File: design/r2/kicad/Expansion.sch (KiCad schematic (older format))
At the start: 25 parts, among them IC1 MC68010P10, IC4 MC68901P, IC6 74174N, IC9 74LS01N, J1 PWR, J3 Conn_02x32_Odd_Even

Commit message: Complete schematic capture for r2
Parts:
- removed IC4: MC68901P, rosco_m68k:DIL48, symbol rosco_m68k-eagle-import:MC68901P
- removed IC6: 74174N, Package_DIP:DIP-16_W7.62mm_Socket_LongPads, symbol rosco_m68k-eagle-import:74174N
- renumbered J1 to J5
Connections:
- net labels removed: A[1..23], D[0..15], IEO
- wire segments 152 -> 78
- no-connect marks 0 -> 1
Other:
- moved on the sheet: C14, C15, C16, C17, C18, C19, C20, C21, C22, C23, C24, C25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

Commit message: Tidy up footprints
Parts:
- removed IC9: 74LS01N, Package_DIP:DIP-14_W7.62mm_Socket_LongPads, symbol rosco_m68k-eagle-import:7401N
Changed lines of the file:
@@
 $Descr A4 11693 8268
 encoding utf-8
-Sheet 3 7
+Sheet 2 7
 Title "ROSCO_M68K GENERAL PURPOSE MC68010 COMPUTER"
 Date "2021-10-08"
@@
 $EndComp
 $Comp
-L rosco_m68k-eagle-import:7401N IC?
-U 5 1 5F6CD650
-P 7500 5250
-AR Path="/5F6CD650" Ref="IC?"  Part="5"
-AR Path="/5E53B952/5F6CD650" Ref="IC?"  Part="5"
-AR Path="/5E53BC83/5F6CD650" Ref="IC9"  Part="5"
-F 0 "IC9" H 7475 5225 59  0000 L BNN
-F 1 "74LS01N" H 7600 5050 59  0001 L BNN
-F 2 "Package_DIP:DIP-14_W7.62mm_Socket_LongPads" H 7500 5250 50  0001 C CNN
-F 3 "" H 7500 5250 50  0001 C CNN
-	5    7500 5250
-	1    0    0    -1
-$EndComp
-$Comp
 L rosco_m68k-eagle-import:C2,5-3 C?
 U 1 1 5F6CD656
@@
 Wire Wire Line
 	3450 5750 3750 5750
-Wire Wire Line
-	7500 5750 7500 5550
 Connection ~ 3450 5750
-Wire Wire Line
-	7500 4950 7500 4650
 Connection ~ 3450 4650
 Wire Wire Line
@@
 L power:GND #PWR0109
 U 1 1 5F7D403D
-P 7500 6050
-F 0 "#PWR0109" H 7500 5800 50  0001 C CNN
-F 1 "GND" H 7505 5877 50  0000 C CNN
-F 2 "" H 7500 6050 50  0001 C CNN
-F 3 "" H 7500 6050 50  0001 C CNN
-	1    7500 6050
-	1    0    0    -1
-$EndComp
-Wire Wire Line
-	7500 6050 7500 5750
-Connection ~ 7500 5750
+P 6850 6050
+F 0 "#PWR0109" H 6850 5800 50  0001 C CNN
+F 1 "GND" H 6855 5877 50  0000 C CNN
+F 2 "" H 6850 6050 50  0001 C CNN
+F 3 "" H 6850 6050 50  0001 C CNN
+	1    6850 6050
+	1    0    0    -1
+$EndComp
+Wire Wire Line
+	6850 6050 6850 5750
 Wire Wire Line
 	750  4300 750  4650
@@
 Connection ~ 6300 4650
 Wire Wire Line
-	6850 4650 7500 4650
-Connection ~ 6850 4650
-Wire Wire Line
 	6850 5350 6850 5750
 Wire Wire Line
-	6850 5750 7500 5750
-Wire Wire Line
 	6850 5750 6300 5750

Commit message: Changes requested by @e2k
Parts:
- added J6: Conn_01x04_Male, Connector_PinHeader_2.54mm:PinHeader_1x04_P2.54mm_Vertical, symbol Connector:Conn_01x04_Male
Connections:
- net A20: now also J6.1 (Pin_1)
- net A21: now also J6.2 (Pin_2)
- net A22: now also J6.3 (Pin_3)
- net A23: now also J6.4 (Pin_4)
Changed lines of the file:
@@
 Wire Wire Line
 	5500 5750 6300 5750
+$Comp
+L Connector:Conn_01x04_Male J6
+U 1 1 61646A1A
+P 3750 3650
+F 0 "J6" H 3858 3931 50  0000 C CNN
+F 1 "Conn_01x04_Male" H 3858 3840 50  0000 C CNN
+F 2 "Connector_PinHeader_2.54mm:PinHeader_1x04_P2.54mm_Vertical" H 3750 3650 50  0001 C CNN
+F 3 "~" H 3750 3650 50  0001 C CNN
+	1    3750 3650
+	1    0    0    -1
+$EndComp
+Text GLabel 3950 3550 2    50   Input ~ 0
+A20
+Text GLabel 3950 3650 2    50   Input ~ 0
+A21
+Text GLabel 3950 3750 2    50   Input ~ 0
+A22
+Text GLabel 3950 3850 2    50   Input ~ 0
+A23
 $EndSCHEMATC

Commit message: Bite the bullet and do IPL properly...
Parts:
- added IC7: 74LS148, Package_DIP:DIP-16_W7.62mm_LongPads, symbol 74xx:74LS148
- added R12, R15, R16, R17, R18: 4K7, rosco_m68k:0207_10, symbol Device:R
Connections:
- net GND: now also IC7.10 (IO), IC7.5 (EI), IC7.8 (GND)
- net IPL0: now also IC7.9 (S0); no longer J3.26 (Pin_26)
- net IPL1: now also IC7.7 (S1); no longer J3.28 (Pin_28)
- net IPL2: now also IC7.6 (S2); no longer J3.30 (Pin_30)
- net VCC: now also IC7.11 (I1), IC7.4 (I7), R12.1, R15.1, R16.1, R17.1, R18.1
- net IRQ3: now reaches J3.14 (Pin_14)
- net IRQ3: now also IC7.13 (I3), R18.2
- new net DUAIRQ: IC7.1 (I4), R16.2
- new net IRQ2: IC7.12 (I2), J3.28 (Pin_28), R15.2
- new net IRQ5: IC7.2 (I5), J3.26 (Pin_26), R17.2
- new net IRQ6: IC7.3 (I6), J3.30 (Pin_30), R12.2
- no-connect marks 1 -> 2
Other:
- moved on the sheet: C19, C21, H1, H2, H3, H4, J5, J6

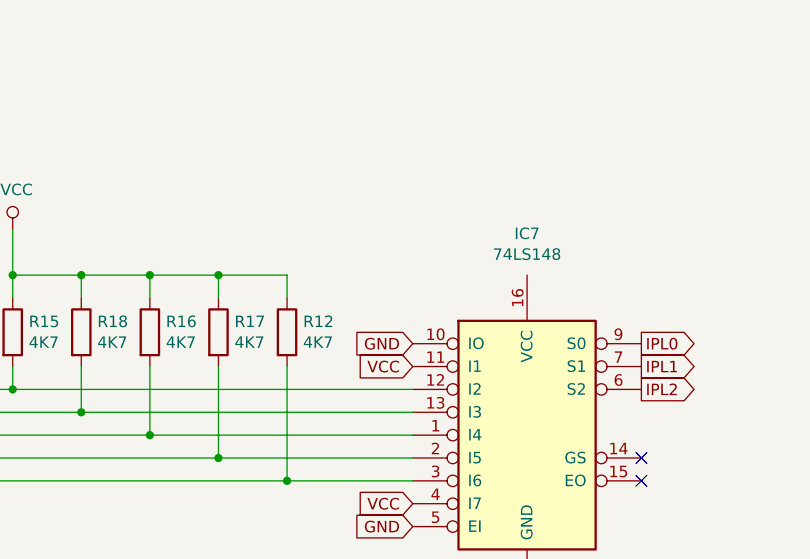
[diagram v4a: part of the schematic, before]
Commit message: Fix unconnected VCC on 148
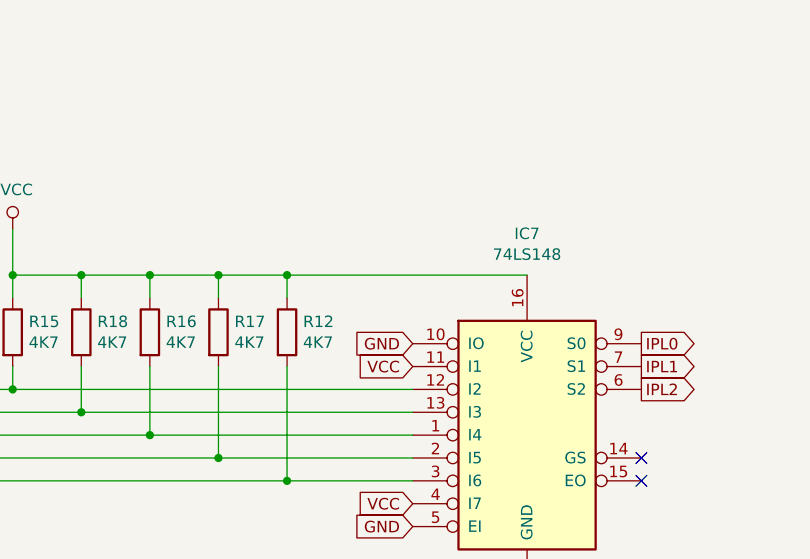
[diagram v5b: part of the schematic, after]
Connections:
- net VCC: now also IC7.16 (VCC)
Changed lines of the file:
@@
 	5850 2900 5300 2900
 Connection ~ 5300 2900
+Wire Wire Line
+	5300 2000 6350 2000
+Connection ~ 5300 2000
 $EndSCHEMATC

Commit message: Super-minor tidy-up
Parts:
- H1, H2, H3, H4: footprint MountingHole:MountingHole_3.2mm_M3 -> MountingHole:MountingHole_3.2mm_M3_Pad; symbol Mechanical:MountingHole -> Mechanical:MountingHole_Pad
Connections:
- net GND: now also H1.1, H2.1, H3.1, H4.1
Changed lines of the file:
@@
 $EndComp
 $Comp
-L Mechanical:MountingHole H?
+L Mechanical:MountingHole_Pad H?
 U 1 1 5FDB083A
 P 1250 3100
@@
 AR Path="/5E53BC83/5FDB083A" Ref="H1"  Part="1"
 F 0 "H1" H 1250 3300 50  0000 C CNN
-F 1 "MountingHole" H 1250 3225 50  0000 C CNN
-F 2 "MountingHole:MountingHole_3.2mm_M3" H 1250 3100 50  0001 C CNN
+F 1 "MountingHole" H 1250 3225 50  0001 C CNN
+F 2 "MountingHole:MountingHole_3.2mm_M3_Pad" H 1250 3100 50  0001 C CNN
 F 3 "~" H 1250 3100 50  0001 C CNN
 	1    1250 3100
@@
 $EndComp
 $Comp
-L Mechanical:MountingHole H?
+L Mechanical:MountingHole_Pad H?
 U 1 1 5FDB0840
-P 1250 3450
+P 1500 3100
 AR Path="/5E53BCCF/5FDB0840" Ref="H?"  Part="1"
 AR Path="/5E53BC83/5FDB0840" Ref="H2"  Part="1"
-F 0 "H2" H 1250 3650 50  0000 C CNN
-F 1 "MountingHole" H 1250 3575 50  0000 C CNN
-F 2 "MountingHole:MountingHole_3.2mm_M3" H 1250 3450 50  0001 C CNN
-F 3 "~" H 1250 3450 50  0001 C CNN
-	1    1250 3450
-	1    0    0    -1
-$EndComp
-$Comp
-L Mechanical:MountingHole H?
+F 0 "H2" H 1500 3300 50  0000 C CNN
+F 1 "MountingHole" H 1500 3225 50  0001 C CNN
+F 2 "MountingHole:MountingHole_3.2mm_M3_Pad" H 1500 3100 50  0001 C CNN
+F 3 "~" H 1500 3100 50  0001 C CNN
+	1    1500 3100
+	1    0    0    -1
+$EndComp
+$Comp
+L Mechanical:MountingHole_Pad H?
 U 1 1 5FDB0846
-P 1250 3800
+P 1800 3100
 AR Path="/5E53BCCF/5FDB0846" Ref="H?"  Part="1"
 AR Path="/5E53BC83/5FDB0846" Ref="H3"  Part="1"
-F 0 "H3" H 1250 4000 50  0000 C CNN
-F 1 "MountingHole" H 1250 3925 50  0000 C CNN
-F 2 "MountingHole:MountingHole_3.2mm_M3" H 1250 3800 50  0001 C CNN
-F 3 "~" H 1250 3800 50  0001 C CNN
-	1    1250 3800
-	1    0    0    -1
-$EndComp
-$Comp
-L Mechanical:MountingHole H?
+F 0 "H3" H 1800 3300 50  0000 C CNN
+F 1 "MountingHole" H 1800 3225 50  0001 C CNN
+F 2 "MountingHole:MountingHole_3.2mm_M3_Pad" H 1800 3100 50  0001 C CNN
+F 3 "~" H 1800 3100 50  0001 C CNN
+	1    1800 3100
+	1    0    0    -1
+$EndComp
+$Comp
+L Mechanical:MountingHole_Pad H?
 U 1 1 5FDB084C
-P 1250 4150
+P 2050 3100
 AR Path="/5E53BCCF/5FDB084C" Ref="H?"  Part="1"
 AR Path="/5E53BC83/5FDB084C" Ref="H4"  Part="1"
-F 0 "H4" H 1250 4350 50  0000 C CNN
-F 1 "MountingHole" H 1250 4275 50  0000 C CNN
-F 2 "MountingHole:MountingHole_3.2mm_M3" H 1250 4150 50  0001 C CNN
-F 3 "~" H 1250 4150 50  0001 C CNN
-	1    1250 4150
+F 0 "H4" H 2050 3300 50  0000 C CNN
+F 1 "MountingHole" H 2050 3225 50  0001 C CNN
+F 2 "MountingHole:MountingHole_3.2mm_M3_Pad" H 2050 3100 50  0001 C CNN
+F 3 "~" H 2050 3100 50  0001 C CNN
+	1    2050 3100
 	1    0    0    -1
 $EndComp
@@
 	5300 2000 6350 2000
 Connection ~ 5300 2000
+Wire Wire Line
+	1250 3200 1250 3300
+Wire Wire Line
+	1250 3300 1500 3300
+Wire Wire Line
+	1650 3300 1650 3400
+Connection ~ 1650 3300
+Wire Wire Line
+	2050 3200 2050 3300
+Wire Wire Line
+	1650 3300 1800 3300
+Wire Wire Line
+	1800 3200 1800 3300
+Connection ~ 1800 3300
+Wire Wire Line
+	1800 3300 2050 3300
+Wire Wire Line
+	1500 3200 1500 3300
+Connection ~ 1500 3300
+Wire Wire Line
+	1500 3300 1650 3300
+$Comp
+L power:GND #PWR?
+U 1 1 61DE23F1
+P 1650 3400
+F 0 "#PWR?" H 1650 3150 50  0001 C CNN
+F 1 "GND" H 1655 3227 50  0000 C CNN
+F 2 "" H 1650 3400 50  0001 C CNN
+F 3 "" H 1650 3400 50  0001 C CNN
+	1    1650 3400
+	1    0    0    -1
+$EndComp
 $EndSCHEMATC
